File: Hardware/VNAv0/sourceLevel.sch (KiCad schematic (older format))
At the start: 26 parts, among them U7 AD8319, U8 SKY12347-362LF, U9 TRF37A75

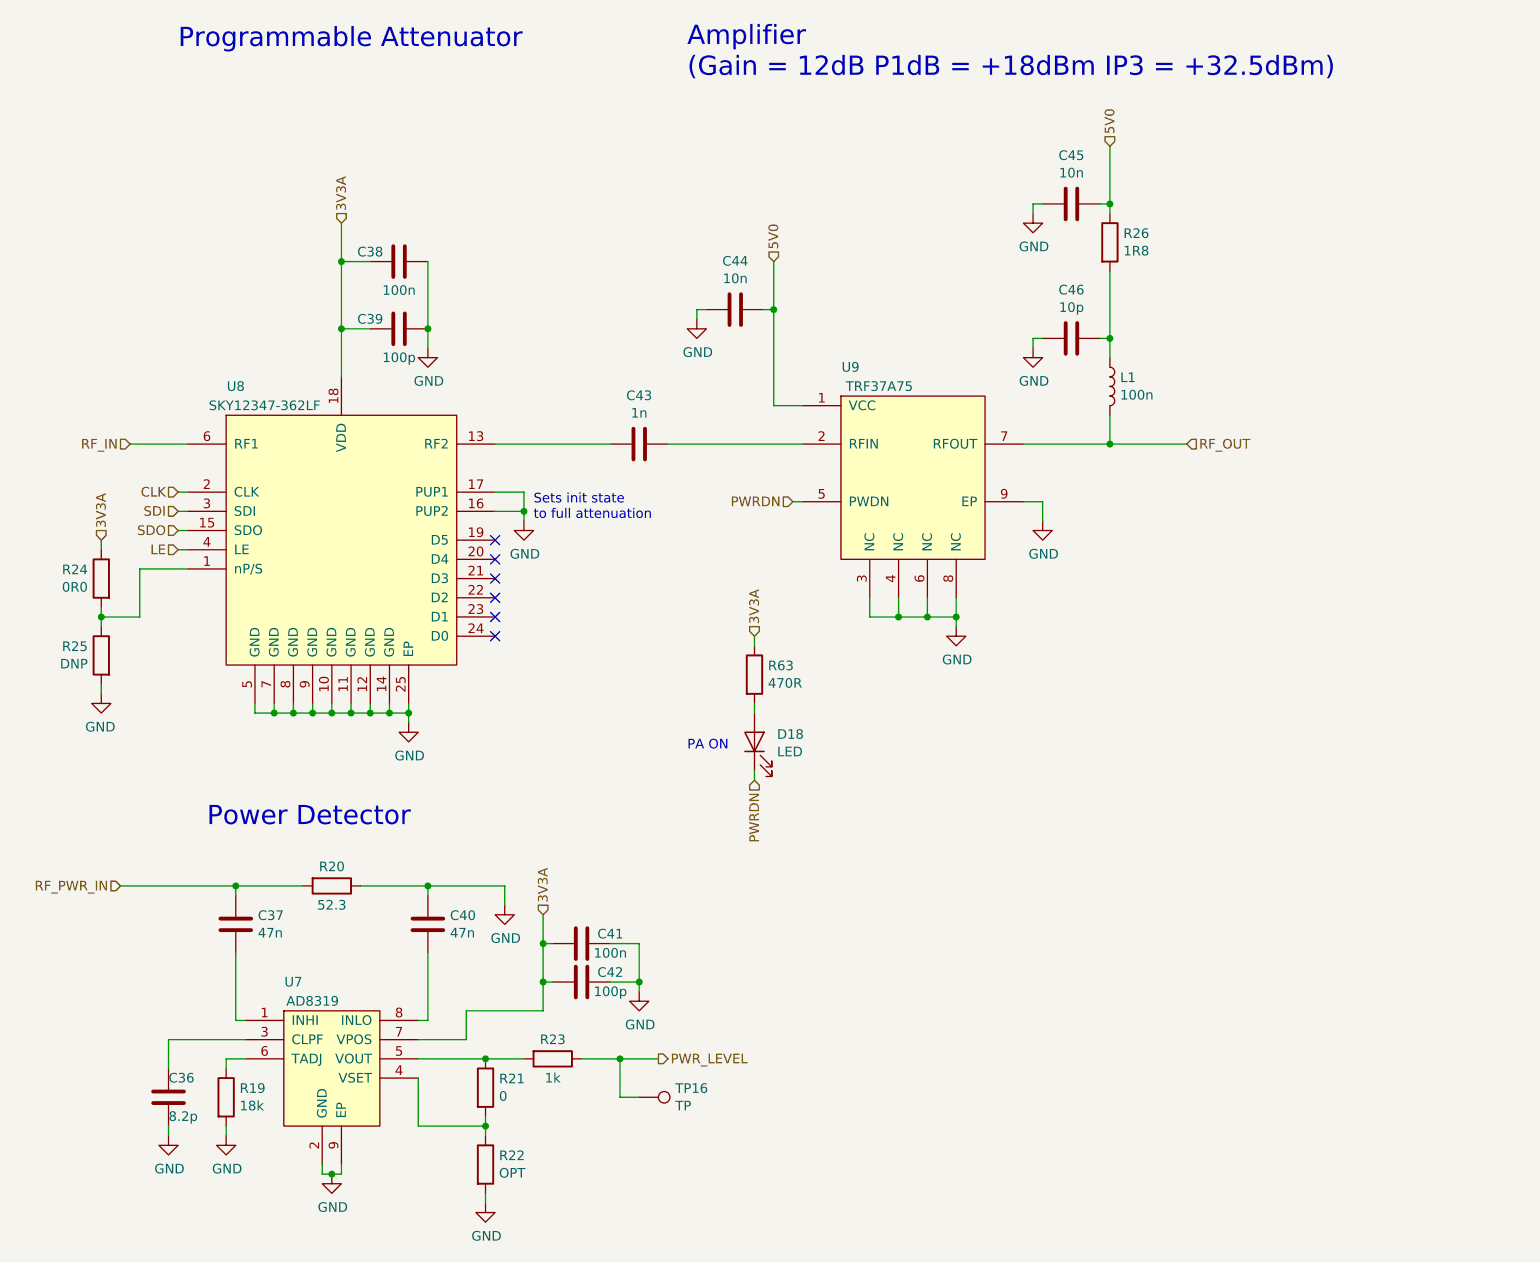
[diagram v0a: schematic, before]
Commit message: tx chain now works, however output power too low
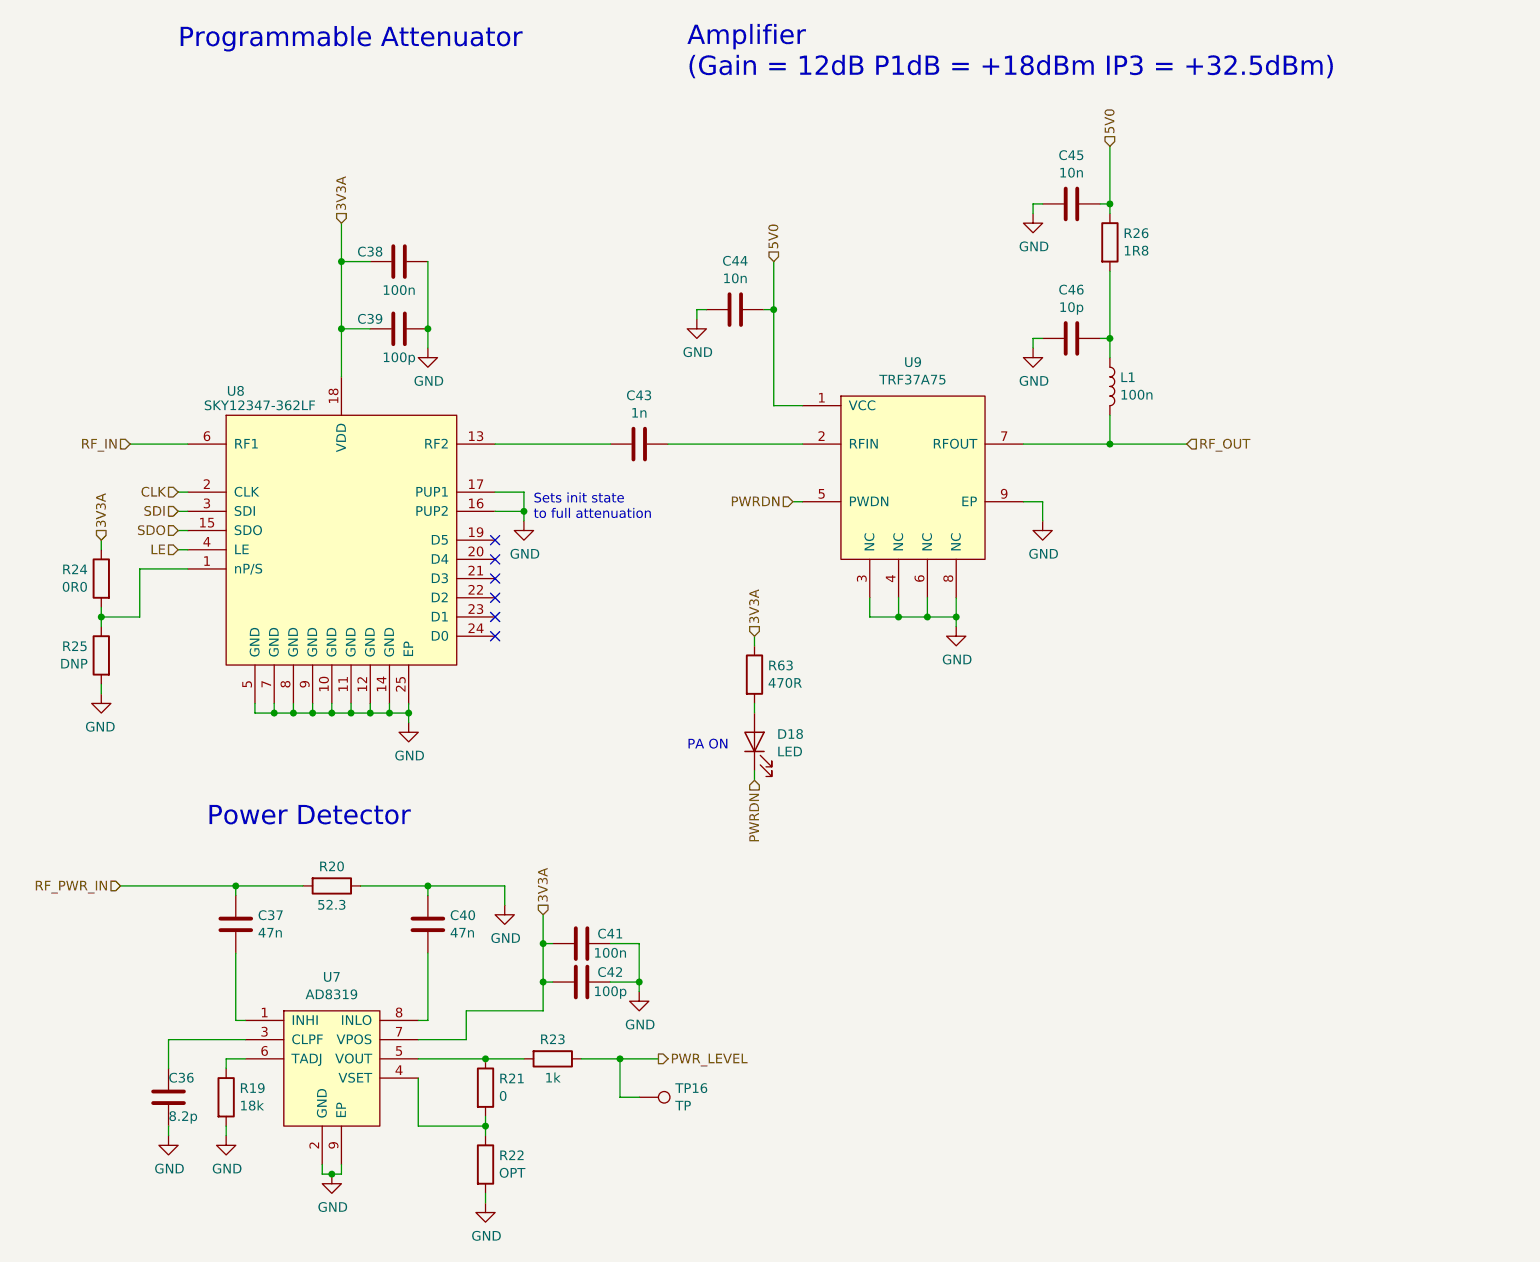
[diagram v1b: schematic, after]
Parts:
- U7: footprint Package_DFN_QFN:DFN-8-1EP_2x3mm_P0.5mm_EP0.61x2.2mm -> (none)
- U9: footprint Package_DFN_QFN:DFN-8-1EP_2x2mm_P0.5mm_EP0.9x1.5mm -> (none)
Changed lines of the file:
@@
-$EndComp
-$Comp
-L VNA_Symbols:AD8319 U7
-U 1 1 5C620E03
-P 3550 6100
-F 0 "U7" H 3350 6500 50  0000 C CNN
-F 1 "AD8319" H 3450 6400 50  0000 C CNN
-F 2 "Package_DFN_QFN:DFN-8-1EP_2x3mm_P0.5mm_EP0.61x2.2mm" H 3550 6250 50  0001 C CNN
-F 3 "" H 3550 6250 50  0001 C CNN
-	1    3550 6100
-	1    0    0    -1
 $EndComp
 $Comp
@@
 Wire Wire Line
 	3600 1950 3600 2300
-$Comp
-L VNA_Symbols:SKY12347-362LF U8
-U 1 1 5CB0A6D7
-P 3600 3350
-F 0 "U8" H 3050 4100 50  0000 C CNN
-F 1 "SKY12347-362LF" H 3200 4000 50  0000 C CNN
-F 2 "Package_DFN_QFN:QFN-24-1EP_4x4mm_P0.5mm_EP2.7x2.7mm_ThermalVias" H 3650 4000 50  0001 C CNN
-F 3 "" H 3650 4000 50  0001 C CNN
-	1    3600 3350
-	1    0    0    -1
-$EndComp
 Wire Wire Line
 	2800 3250 2750 3250
@@
 Wire Wire Line
 	6350 3700 6350 3800
-$Comp
-L VNA_Symbols:TRF37A75 U9
-U 1 1 5C86DCF3
-P 6550 3050
-F 0 "U9" H 6250 3600 50  0000 C CNN
-F 1 "TRF37A75" H 6400 3500 50  0000 C CNN
-F 2 "Package_DFN_QFN:DFN-8-1EP_2x2mm_P0.5mm_EP0.9x1.5mm" H 6800 3300 50  0001 C CNN
-F 3 "" H 6800 3300 50  0001 C CNN
-	1    6550 3050
-	1    0    0    -1
-$EndComp
 Text HLabel 5750 4650 3    50   Input ~ 0
 PWRDN
@@
 	3150 4300 3150 4250
 Connection ~ 3250 4300
+$Comp
+L VNA_Symbols:SKY12347-362LF U8
+U 1 1 5D16EEBF
+P 3600 3350
+F 0 "U8" H 3050 4075 50  0000 C CNN
+F 1 "SKY12347-362LF" H 3175 4000 50  0000 C CNN
+F 2 "Package_DFN_QFN:QFN-24-1EP_4x4mm_P0.5mm_EP2.7x2.7mm_ThermalVias" H 3650 4000 50  0001 C CNN
+F 3 "" H 3650 4000 50  0001 C CNN
+	1    3600 3350
+	1    0    0    -1
+$EndComp
+$Comp
+L VNA_Symbols:AD8319 U7
+U 1 1 5D170444
+P 3550 6100
+F 0 "U7" H 3550 6525 50  0000 C CNN
+F 1 "AD8319" H 3550 6434 50  0000 C CNN
+F 2 "" H 3550 6250 50  0001 C CNN
+F 3 "" H 3550 6250 50  0001 C CNN
+	1    3550 6100
+	1    0    0    -1
+$EndComp
+$Comp
+L VNA_Symbols:TRF37A75 U9
+U 1 1 5D170F28
+P 6550 3050
+F 0 "U9" H 6575 3625 50  0000 C CNN
+F 1 "TRF37A75" H 6575 3534 50  0000 C CNN
+F 2 "" H 6800 3300 50  0001 C CNN
+F 3 "" H 6800 3300 50  0001 C CNN
+	1    6550 3050
+	1    0    0    -1
+$EndComp
 $EndSCHEMATC
